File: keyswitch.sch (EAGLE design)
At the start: 45 parts

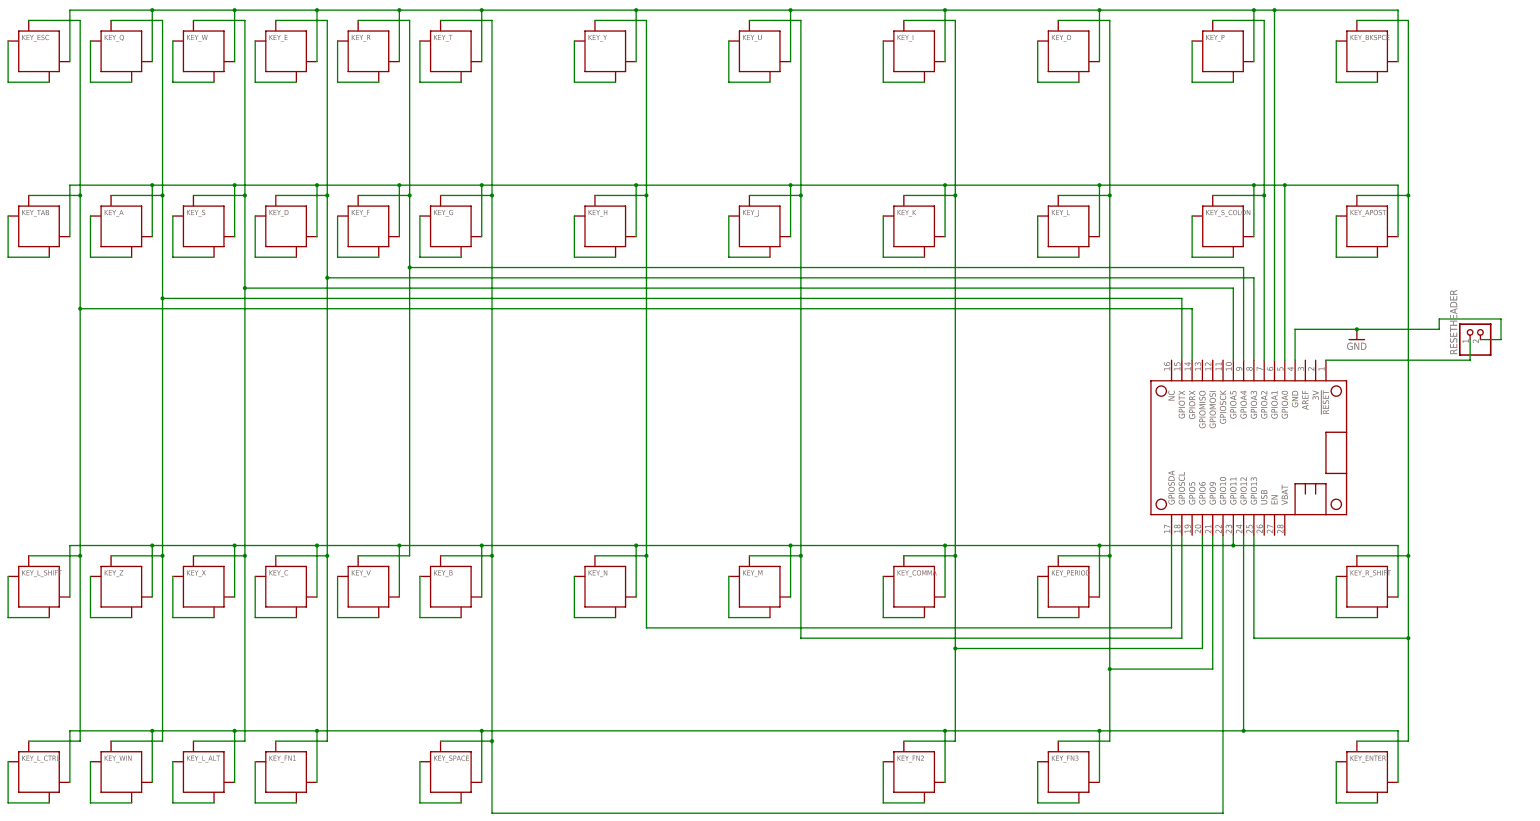
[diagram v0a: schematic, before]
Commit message: modified to remove vias
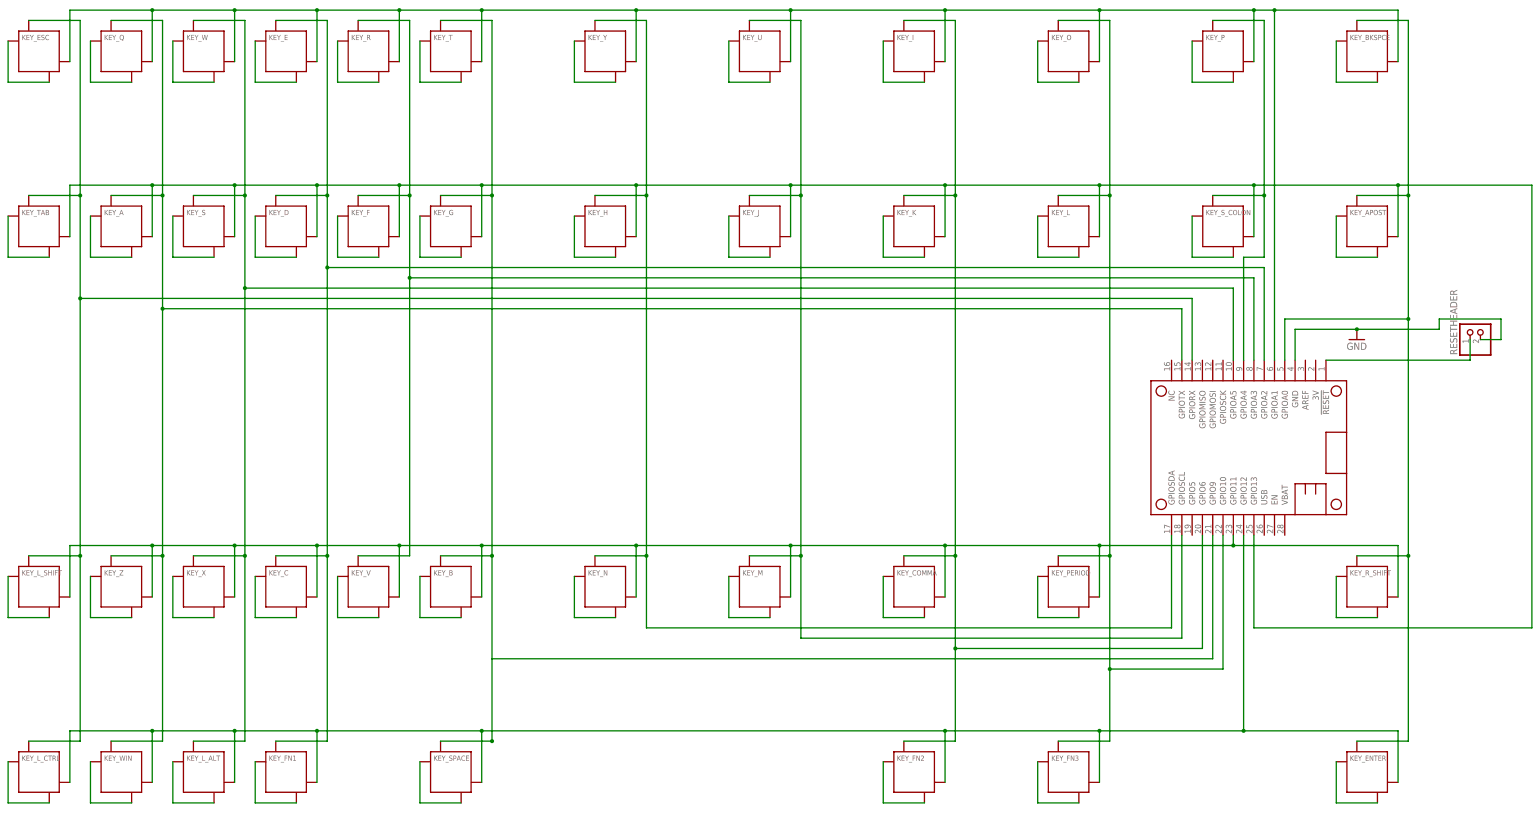
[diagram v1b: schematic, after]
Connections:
- net N$35: now also FEATHER.GPIOA2; no longer FEATHER.GPIOA3
- net N$46: now also FEATHER.GPIO9; no longer FEATHER.GPIO10
- net N$49: now also FEATHER.GPIOA3; no longer FEATHER.GPIOA4
- net N$52: now also FEATHER.GPIO10; no longer FEATHER.GPIO9
- net N$55: now also FEATHER.GPIOA4; no longer FEATHER.GPIOA2
- net N$56: now also FEATHER.GPIOA0; no longer FEATHER.GPIO13
- net N$72: now also FEATHER.GPIO13; no longer FEATHER.GPIOA0
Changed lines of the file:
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@@
 <wire x1="-78.74" y1="101.6" x2="-78.74" y2="58.42" width="0.1524" layer="91"/>
 <wire x1="-78.74" y1="-30.48" x2="-78.74" y2="-76.2" width="0.1524" layer="91"/>
-<wire x1="-78.74" y1="-30.48" x2="-78.74" y2="33.02" width="0.1524" layer="91"/>
-<wire x1="-78.74" y1="33.02" x2="-78.74" y2="58.42" width="0.1524" layer="91"/>
+<wire x1="-78.74" y1="-30.48" x2="-78.74" y2="30.48" width="0.1524" layer="91"/>
+<wire x1="-78.74" y1="30.48" x2="-78.74" y2="58.42" width="0.1524" layer="91"/>
 <wire x1="-91.44" y1="101.6" x2="-78.74" y2="101.6" width="0.1524" layer="91"/>
 <pinref part="KEY_A" gate="G$1" pin="P1"/>
@@
 <pinref part="KEY_WIN" gate="G$1" pin="P1"/>
 <wire x1="-91.44" y1="-76.2" x2="-78.74" y2="-76.2" width="0.1524" layer="91"/>
-<wire x1="-78.74" y1="33.02" x2="172.72" y2="33.02" width="0.1524" layer="91"/>
-<junction x="-78.74" y="33.02"/>
+<wire x1="-78.74" y1="30.48" x2="172.72" y2="30.48" width="0.1524" layer="91"/>
+<junction x="-78.74" y="30.48"/>
 <pinref part="FEATHER" gate="G$1" pin="GPIOTX"/>
-<wire x1="172.72" y1="17.78" x2="172.72" y2="33.02" width="0.1524" layer="91"/>
+<wire x1="172.72" y1="17.78" x2="172.72" y2="30.48" width="0.1524" layer="91"/>
 </segment>
 </net>
@@
 <net name="N$49" class="0">
 <segment>
-<wire x1="-17.78" y1="-30.48" x2="-17.78" y2="40.64" width="0.1524" layer="91"/>
-<wire x1="-17.78" y1="40.64" x2="-17.78" y2="58.42" width="0.1524" layer="91"/>
+<wire x1="-17.78" y1="-30.48" x2="-17.78" y2="38.1" width="0.1524" layer="91"/>
+<wire x1="-17.78" y1="38.1" x2="-17.78" y2="58.42" width="0.1524" layer="91"/>
 <wire x1="-17.78" y1="58.42" x2="-17.78" y2="101.6" width="0.1524" layer="91"/>
 <pinref part="KEY_R" gate="G$1" pin="P1"/>
@@
 <pinref part="KEY_V" gate="G$1" pin="P1"/>
 <wire x1="-30.48" y1="-30.48" x2="-17.78" y2="-30.48" width="0.1524" layer="91"/>
-<wire x1="-17.78" y1="40.64" x2="187.96" y2="40.64" width="0.1524" layer="91"/>
-<junction x="-17.78" y="40.64"/>
-<pinref part="FEATHER" gate="G$1" pin="GPIOA4"/>
-<wire x1="187.96" y1="17.78" x2="187.96" y2="40.64" width="0.1524" layer="91"/>
+<wire x1="-17.78" y1="38.1" x2="190.5" y2="38.1" width="0.1524" layer="91"/>
+<junction x="-17.78" y="38.1"/>
+<pinref part="FEATHER" gate="G$1" pin="GPIOA3"/>
+<wire x1="190.5" y1="38.1" x2="190.5" y2="17.78" width="0.1524" layer="91"/>
 </segment>
 </net>
@@
 <pinref part="KEY_S_COLON" gate="G$1" pin="P1"/>
 <wire x1="180.34" y1="58.42" x2="193.04" y2="58.42" width="0.1524" layer="91"/>
-<pinref part="FEATHER" gate="G$1" pin="GPIOA2"/>
-<wire x1="193.04" y1="58.42" x2="193.04" y2="17.78" width="0.1524" layer="91"/>
+<wire x1="193.04" y1="58.42" x2="193.04" y2="43.18" width="0.1524" layer="91"/>
+<wire x1="193.04" y1="43.18" x2="187.96" y2="43.18" width="0.1524" layer="91"/>
 <junction x="193.04" y="58.42"/>
+<pinref part="FEATHER" gate="G$1" pin="GPIOA4"/>
+<wire x1="187.96" y1="43.18" x2="187.96" y2="17.78" width="0.1524" layer="91"/>
 </segment>
 </net>
 <net name="N$56" class="0">
 <segment>
-<wire x1="228.6" y1="-76.2" x2="228.6" y2="-50.8" width="0.1524" layer="91"/>
-<wire x1="228.6" y1="-50.8" x2="228.6" y2="-30.48" width="0.1524" layer="91"/>
-<wire x1="228.6" y1="-30.48" x2="228.6" y2="58.42" width="0.1524" layer="91"/>
+<wire x1="228.6" y1="-76.2" x2="228.6" y2="-30.48" width="0.1524" layer="91"/>
+<wire x1="228.6" y1="-30.48" x2="228.6" y2="27.94" width="0.1524" layer="91"/>
+<wire x1="228.6" y1="27.94" x2="228.6" y2="58.42" width="0.1524" layer="91"/>
 <wire x1="228.6" y1="58.42" x2="228.6" y2="101.6" width="0.1524" layer="91"/>
 <pinref part="KEY_BKSPCE" gate="G$1" pin="P1"/>
@@
 <pinref part="KEY_ENTER" gate="G$1" pin="P1"/>
 <wire x1="215.9" y1="-76.2" x2="228.6" y2="-76.2" width="0.1524" layer="91"/>
-<pinref part="FEATHER" gate="G$1" pin="GPIO13"/>
-<wire x1="228.6" y1="-50.8" x2="190.5" y2="-50.8" width="0.1524" layer="91"/>
-<wire x1="190.5" y1="-50.8" x2="190.5" y2="-25.4" width="0.1524" layer="91"/>
-<junction x="228.6" y="-50.8"/>
+<pinref part="FEATHER" gate="G$1" pin="GPIOA0"/>
+<wire x1="228.6" y1="27.94" x2="198.12" y2="27.94" width="0.1524" layer="91"/>
+<wire x1="198.12" y1="27.94" x2="198.12" y2="17.78" width="0.1524" layer="91"/>
+<junction x="228.6" y="27.94"/>
 </segment>
 </net>
@@
 <segment>
 <wire x1="-99.06" y1="101.6" x2="-99.06" y2="58.42" width="0.1524" layer="91"/>
-<wire x1="-99.06" y1="58.42" x2="-99.06" y2="30.48" width="0.1524" layer="91"/>
-<wire x1="-99.06" y1="30.48" x2="-99.06" y2="-30.48" width="0.1524" layer="91"/>
+<wire x1="-99.06" y1="58.42" x2="-99.06" y2="33.02" width="0.1524" layer="91"/>
+<wire x1="-99.06" y1="33.02" x2="-99.06" y2="-30.48" width="0.1524" layer="91"/>
 <wire x1="-99.06" y1="-30.48" x2="-99.06" y2="-76.2" width="0.1524" layer="91"/>
 <pinref part="KEY_ESC" gate="G$1" pin="P1"/>
@@
 <wire x1="-111.76" y1="58.42" x2="-99.06" y2="58.42" width="0.1524" layer="91"/>
 <junction x="-99.06" y="58.42"/>
-<wire x1="-99.06" y1="30.48" x2="175.26" y2="30.48" width="0.1524" layer="91"/>
-<junction x="-99.06" y="30.48"/>
+<wire x1="-99.06" y1="33.02" x2="175.26" y2="33.02" width="0.1524" layer="91"/>
+<junction x="-99.06" y="33.02"/>
 <pinref part="FEATHER" gate="G$1" pin="GPIORX"/>
-<wire x1="175.26" y1="30.48" x2="175.26" y2="17.78" width="0.1524" layer="91"/>
+<wire x1="175.26" y1="33.02" x2="175.26" y2="17.78" width="0.1524" layer="91"/>
 </segment>
 </net>
@@
 <net name="N$46" class="0">
 <segment>
-<wire x1="2.54" y1="-76.2" x2="2.54" y2="-30.48" width="0.1524" layer="91"/>
+<wire x1="2.54" y1="-55.88" x2="2.54" y2="-30.48" width="0.1524" layer="91"/>
 <wire x1="2.54" y1="-30.48" x2="2.54" y2="58.42" width="0.1524" layer="91"/>
 <wire x1="2.54" y1="58.42" x2="2.54" y2="101.6" width="0.1524" layer="91"/>
@@
 <pinref part="KEY_SPACE" gate="G$1" pin="P1"/>
 <wire x1="-10.16" y1="-76.2" x2="2.54" y2="-76.2" width="0.1524" layer="91"/>
-<pinref part="FEATHER" gate="G$1" pin="GPIO10"/>
-<wire x1="182.88" y1="-93.98" x2="182.88" y2="-25.4" width="0.1524" layer="91"/>
-<wire x1="2.54" y1="-76.2" x2="2.54" y2="-93.98" width="0.1524" layer="91"/>
-<wire x1="2.54" y1="-93.98" x2="182.88" y2="-93.98" width="0.1524" layer="91"/>
+<wire x1="2.54" y1="-76.2" x2="2.54" y2="-55.88" width="0.1524" layer="91"/>
+<wire x1="2.54" y1="-55.88" x2="180.34" y2="-55.88" width="0.1524" layer="91"/>
 <junction x="2.54" y="-76.2"/>
+<pinref part="FEATHER" gate="G$1" pin="GPIO9"/>
+<wire x1="180.34" y1="-55.88" x2="180.34" y2="-25.4" width="0.1524" layer="91"/>
 </segment>
 </net>
@@
 <pinref part="KEY_FN3" gate="G$1" pin="P1"/>
 <wire x1="142.24" y1="-76.2" x2="154.94" y2="-76.2" width="0.1524" layer="91"/>
-<pinref part="FEATHER" gate="G$1" pin="GPIO9"/>
-<wire x1="154.94" y1="-58.42" x2="180.34" y2="-58.42" width="0.1524" layer="91"/>
-<wire x1="180.34" y1="-58.42" x2="180.34" y2="-25.4" width="0.1524" layer="91"/>
+<wire x1="154.94" y1="-58.42" x2="182.88" y2="-58.42" width="0.1524" layer="91"/>
 <junction x="154.94" y="-58.42"/>
+<pinref part="FEATHER" gate="G$1" pin="GPIO10"/>
+<wire x1="182.88" y1="-58.42" x2="182.88" y2="-25.4" width="0.1524" layer="91"/>
 </segment>
 </net>
@@
 <wire x1="-38.1" y1="58.42" x2="-38.1" y2="101.6" width="0.1524" layer="91"/>
 <wire x1="-38.1" y1="-76.2" x2="-38.1" y2="-30.48" width="0.1524" layer="91"/>
-<wire x1="-38.1" y1="-30.48" x2="-38.1" y2="38.1" width="0.1524" layer="91"/>
+<wire x1="-38.1" y1="-30.48" x2="-38.1" y2="40.64" width="0.1524" layer="91"/>
 <pinref part="KEY_E" gate="G$1" pin="P1"/>
-<wire x1="-38.1" y1="38.1" x2="-38.1" y2="58.42" width="0.1524" layer="91"/>
+<wire x1="-38.1" y1="40.64" x2="-38.1" y2="58.42" width="0.1524" layer="91"/>
 <wire x1="-50.8" y1="101.6" x2="-38.1" y2="101.6" width="0.1524" layer="91"/>
 <pinref part="KEY_D" gate="G$1" pin="P1"/>
@@
 <wire x1="-50.8" y1="-76.2" x2="-38.1" y2="-76.2" width="0.1524" layer="91"/>
 <junction x="-38.1" y="58.42"/>
-<wire x1="-38.1" y1="38.1" x2="190.5" y2="38.1" width="0.1524" layer="91"/>
-<junction x="-38.1" y="38.1"/>
-<pinref part="FEATHER" gate="G$1" pin="GPIOA3"/>
-<wire x1="190.5" y1="38.1" x2="190.5" y2="17.78" width="0.1524" layer="91"/>
+<wire x1="-38.1" y1="40.64" x2="193.04" y2="40.64" width="0.1524" layer="91"/>
+<junction x="-38.1" y="40.64"/>
+<pinref part="FEATHER" gate="G$1" pin="GPIOA2"/>
+<wire x1="193.04" y1="40.64" x2="193.04" y2="17.78" width="0.1524" layer="91"/>
 </segment>
 </net>
@@
 <pinref part="KEY_APOST" gate="G$1" pin="D-"/>
 <wire x1="226.06" y1="48.26" x2="226.06" y2="60.96" width="0.1524" layer="91"/>
-<wire x1="226.06" y1="60.96" x2="198.12" y2="60.96" width="0.1524" layer="91"/>
-<pinref part="FEATHER" gate="G$1" pin="GPIOA0"/>
-<wire x1="198.12" y1="60.96" x2="190.5" y2="60.96" width="0.1524" layer="91"/>
-<wire x1="198.12" y1="17.78" x2="198.12" y2="60.96" width="0.1524" layer="91"/>
-<junction x="198.12" y="60.96"/>
-</segment>
-</net>
+<wire x1="226.06" y1="60.96" x2="190.5" y2="60.96" width="0.1524" layer="91"/>
+<wire x1="226.06" y1="60.96" x2="259.08" y2="60.96" width="0.1524" layer="91"/>
+<wire x1="259.08" y1="60.96" x2="259.08" y2="-48.26" width="0.1524" layer="91"/>
+<junction x="226.06" y="60.96"/>
+<pinref part="FEATHER" gate="G$1" pin="GPIO13"/>
+<wire x1="259.08" y1="-48.26" x2="190.5" y2="-48.26" width="0.1524" layer="91"/>
+<wire x1="190.5" y1="-48.26" x2="190.5" y2="-25.4" width="0.1524" layer="91"/>
+</segment>
+</net>
